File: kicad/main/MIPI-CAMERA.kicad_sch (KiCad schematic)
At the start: 11 parts

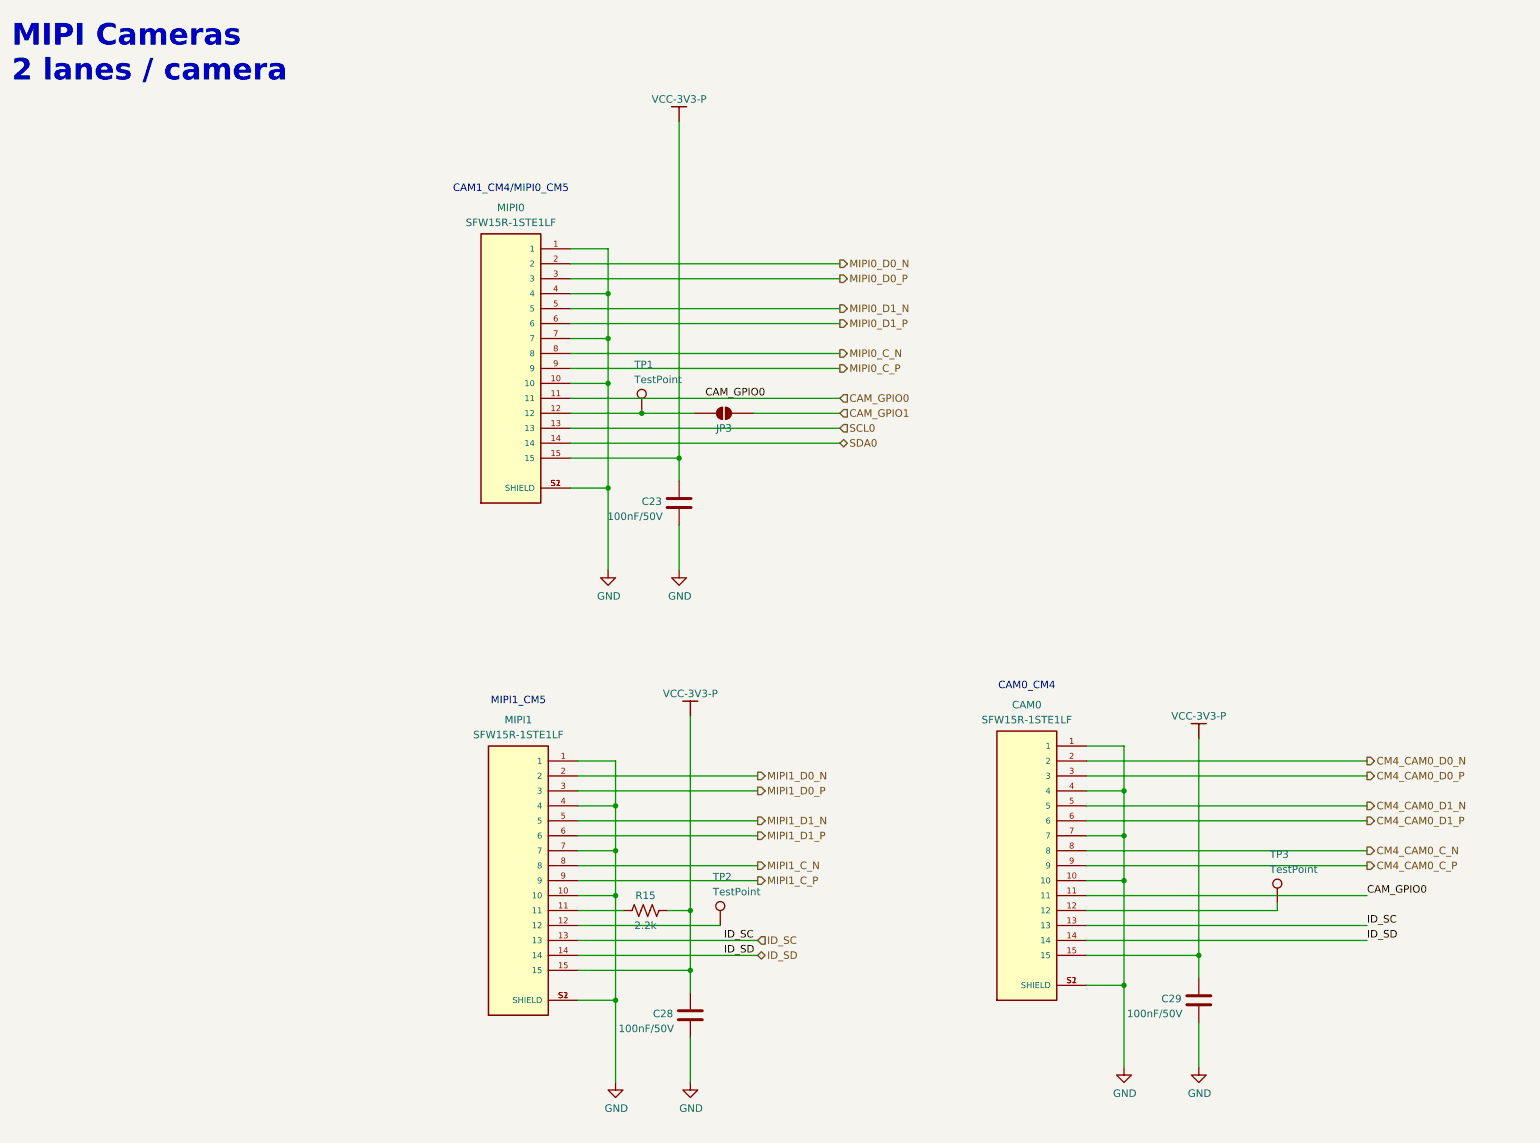
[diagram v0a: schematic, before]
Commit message: Cliff/bumpers connector
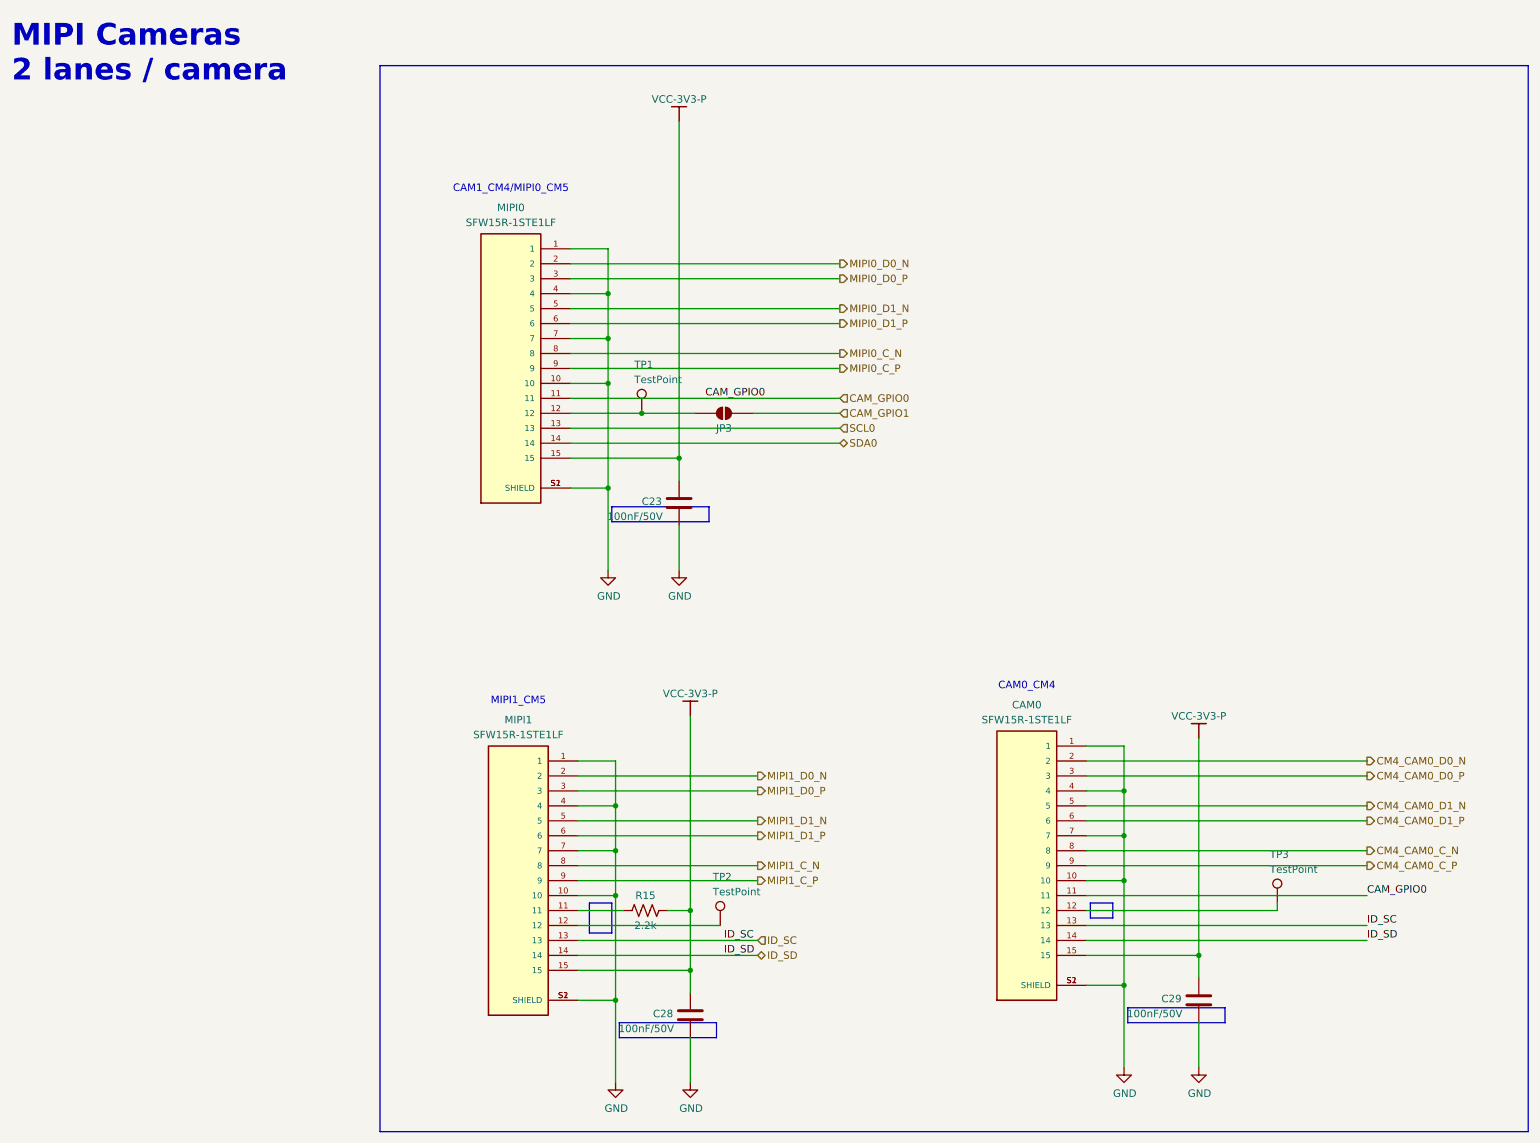
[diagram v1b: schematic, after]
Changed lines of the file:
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@@
 	(generator_version "10.0")
 	(paper "A2")
+	(rectangle
+		(start 254 267.97)
+		(end 257.81 273.05)
+		(stroke
+			(width 0)
+			(type solid)
+		)
+		(fill
+			(type color)
+			(color 132 0 0 1)
+		)
+	)
+	(rectangle
+		(start 259.08 288.29)
+		(end 275.59 290.83)
+		(stroke
+			(width 0)
+			(type solid)
+		)
+		(fill
+			(type color)
+			(color 132 0 0 1)
+		)
+	)
+	(rectangle
+		(start 345.44 285.75)
+		(end 361.95 288.29)
+		(stroke
+			(width 0)
+			(type solid)
+		)
+		(fill
+			(type color)
+			(color 132 0 0 1)
+		)
+	)
+	(rectangle
+		(start 218.44 125.73)
+		(end 413.4586 306.7926)
+		(stroke
+			(width 0)
+			(type solid)
+		)
+		(fill
+			(type color)
+			(color 0 72 0 1)
+		)
+	)
+	(rectangle
+		(start 257.81 200.66)
+		(end 274.32 203.2)
+		(stroke
+			(width 0)
+			(type solid)
+		)
+		(fill
+			(type color)
+			(color 132 0 0 1)
+		)
+	)
+	(rectangle
+		(start 339.09 267.97)
+		(end 342.9 270.51)
+		(stroke
+			(width 0)
+			(type solid)
+		)
+		(fill
+			(type color)
+			(color 132 0 0 1)
+		)
+	)
 	(text "CAM1_CM4/MIPI0_CM5"
 		(exclude_from_sim no)
@@
 			(justify left)
 		)
-		(property "Net Class" ""
+		(property "Netclass" ""
 			(at 282.575 262.89 0)
 			(show_name no)
@@
 			(justify left)
 		)
-		(property "Net Class" ""
+		(property "Netclass" ""
 			(at 296.545 175.895 0)
 			(show_name no)

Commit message: Second review round
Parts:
- removed C23, C28, C29: 100nF/50V, Capacitor_SMD:C_0603_1608Metric, symbol Device:C
- removed R15: 2.2k, Resistor_SMD:R_0603_1608Metric, symbol Device:R_US
- removed TP1, TP2: TestPoint, TestPoint:TestPoint_Pad_D2.0mm, symbol Connector:TestPoint
- added C20, C23, C24: 10uF/25V, Capacitor_SMD:C_0603_1608Metric, symbol Device:C_Small
- added JP4, JP5: (no value), Jumper:SolderJumper-2_P1.3mm_Open_RoundedPad1.0x1.5mm, symbol Jumper:SolderJumper_2_Open
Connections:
- net GND: now also C20.2, C23.2, C24.2
- net VCC-3V3-P: now also C20.1, C23.1, C24.1
- net IO1: now reaches JP3.1 (A), MIPI0.12
- net IO1: now also CAM0.12, TP3.1
- net at MIPI1.12: now also JP5.1 (A)
- net at MIPI1.11: now also JP4.1 (A)
- new net MIPI1_IO0: JP4.2 (B)
- new net MIPI1_IO1: JP5.2 (B)

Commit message: STM32 power rail switch
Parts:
- C20, C23, C24: value 10uF/25V -> 10uF/6.3V; LCSC C96446 -> C1691
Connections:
- net VCC-3V3-P renamed VCC-3V3-REG
